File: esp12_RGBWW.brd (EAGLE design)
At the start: 49.5 x 50.5 mm, 22 parts

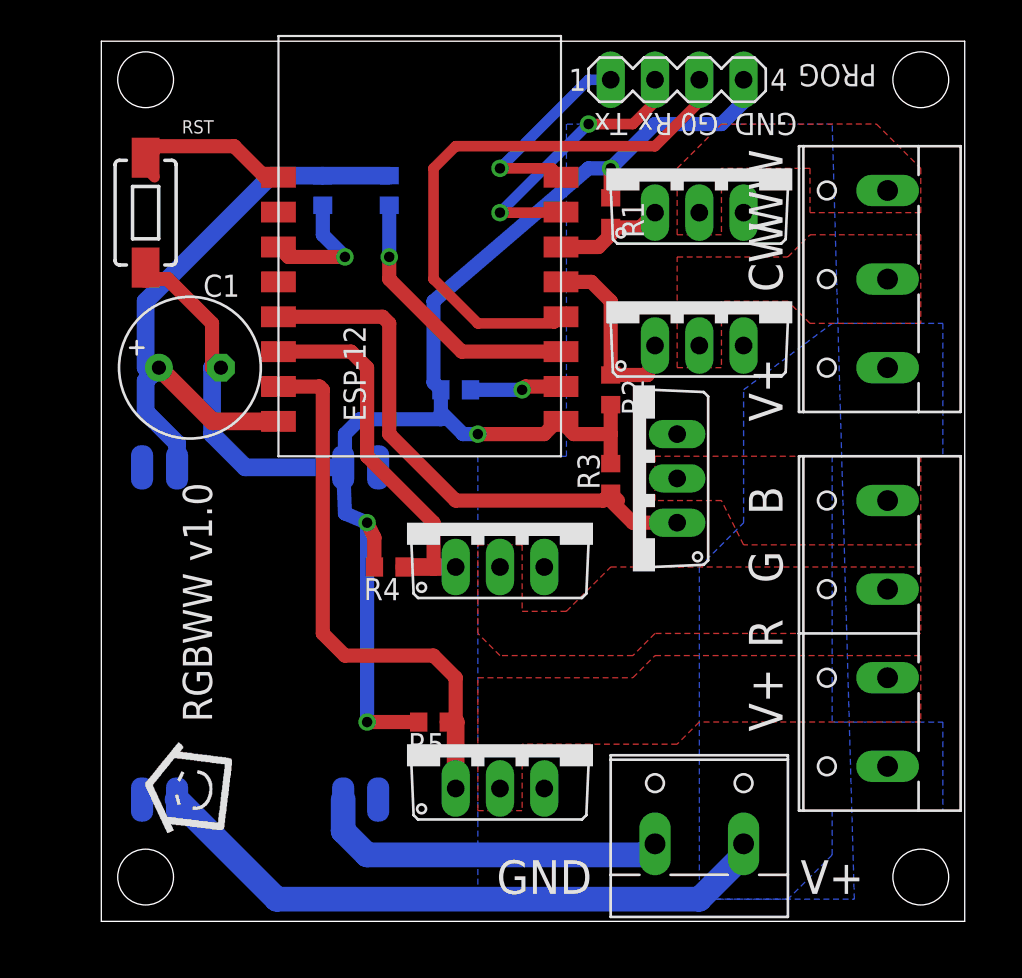
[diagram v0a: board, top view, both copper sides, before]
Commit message: added ADC and updated board layout
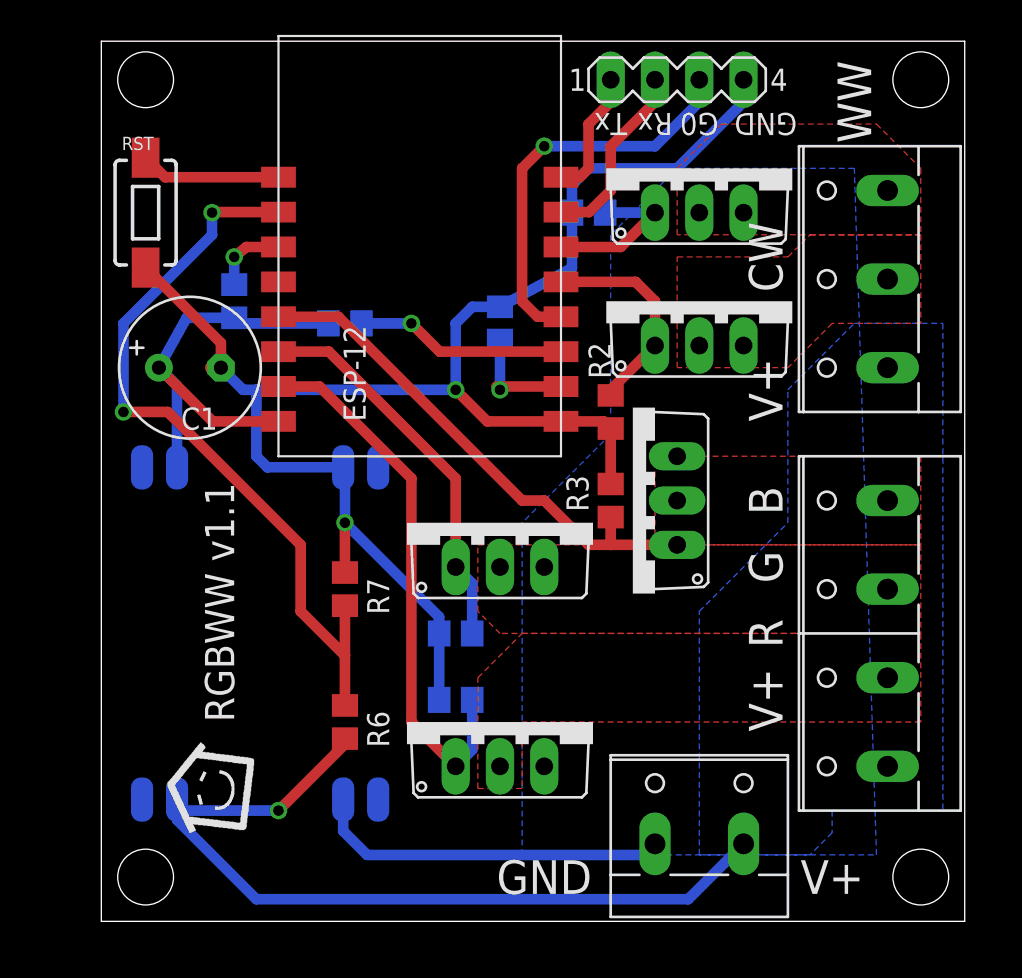
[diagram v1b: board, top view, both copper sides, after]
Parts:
- added R6: 10k, rcl:R0805
- added R7: 1k, rcl:R0805
- CH_PD, GPIO15, GPIO2, R1, R2, R3, R4, R5: device rcl:R0603 -> rcl:R0805
- moved CH_PD 8.13 mm to (7.62, 35.6), turned to 270 degrees
- moved GPIO2 8.03 mm to (14.0, 34.3), turned to 0 degrees
- moved R4 5.39 mm to (20.3, 16.5), flipped to the bottom, turned to 0 degrees
- moved GPIO15 4.58 mm to (22.9, 34.3), turned to 90 degrees
- moved R5 1.80 mm to (20.3, 12.7), flipped to the bottom, turned to 0 degrees
- moved U$1 1.27 mm to (8.89, 5.08)
- moved IRLZ44N-B 1.27 mm to (30.5, 24.1)
- moved IRLZ44N-R 1.27 mm to (22.9, 11.4)
- moved R1 1.27 mm to (27.9, 40.6), flipped to the bottom, turned to 180 degrees
- moved R2 1.27 mm to (29.2, 29.2)
- moved R3 1.27 mm to (29.2, 24.1)
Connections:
- new net N$21: ESP-12.10, R6.1, R7.2
- net +12V: now also R6.2
- net GND3.3V: now also R7.1
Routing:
- net N$21: track 0.00 -> 43.8 mm, vias 0 -> 2
- net +12V: track 36.5 -> 48.4 mm, vias 0 -> 1
- net N$20: track 36.2 -> 25.8 mm
- net N$9: track 33.0 -> 23.2 mm, vias 0 -> 1
- net N$5: track 16.3 -> 10.8 mm, vias 2 -> 0
- net N$8: track 12.2 -> 7.40 mm, vias 1 -> 0
- net GND3.3V: track 96.4 -> 91.8 mm, vias 4 -> 2
- net N$3: track 15.8 -> 12.1 mm
- net N$2: track 7.53 -> 4.33 mm
- net N$13: track 32.7 -> 29.9 mm
- net N$14: track 6.45 -> 9.07 mm
- net N$12: track 9.96 -> 8.08 mm
- net N$7: track 5.27 -> 6.82 mm
- net R4: track 21.4 -> 22.5 mm
- net N$1: track 11.4 -> 12.3 mm
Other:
- board text added: "RGBWW v1.1"
- board text removed: "RGBWW v1.0"

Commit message: v1.2
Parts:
- added C2: 100n, rcl:C0805
- added C3: (no value), resistor:E2,5-6
- added REST: 10k, rcl:R0805
- moved IRLZ44N-R 11.7 mm to (34.3, 14.0)
- moved IRLZ44N-G 11.5 mm to (34.3, 21.6)
- moved C1 10.2 mm to (5.08, 21.6), turned to 270 degrees
- moved VCC 10.2 mm to (24.1, 5.08)
- moved U$1 9.92 mm to (1.27, 11.4), turned to 0 degrees
- moved DC_CONVERTER 9.16 mm to (16.5, 21.6)
- moved R4 7.41 mm to (26.7, 20.3), flipped to the top, turned to 90 degrees
- moved R5 6.84 mm to (26.7, 15.2), flipped to the top
- moved R6 6.48 mm to (12.7, 17.8), turned to 180 degrees
- moved IRLZ44N-B 6.35 mm to (34.3, 29.2), turned to 0 degrees
- moved R2 4.58 mm to (26.7, 33.0)
- moved PROG 3.81 mm to (29.2, 48.3)
- moved ESP-12 3.81 mm to (6.35, 26.7)
- moved GPIO15 2.84 mm to (20.3, 35.6), turned to 180 degrees
- moved R7 2.84 mm to (12.7, 21.6), turned to 0 degrees
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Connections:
- removed net GND3.3V: C1.-, DC_CONVERTER.OUT-(2), ESP-12.1, GPIO15.2, PROG.4, R1.1, R2.2, R3.2, R4.2, R5.2, R7.1, RST.1
- removed net N$20: C1.+, CH_PD.2, DC_CONVERTER.OUT+(1), ESP-12.16, GPIO2.2
- new net +3V3: C1.+, C2.2, CH_PD.2, DC_CONVERTER.OUT+(1), ESP-12.16, GPIO2.2, REST.1
- net +12V: now also C3.+
- net GND: now also C1.-, C2.1, C3.-, DC_CONVERTER.OUT-(2), ESP-12.1, GPIO15.2, PROG.4, R1.1, R2.2, R3.2, R4.2, R5.2, R7.1, RST.1
- net N$12: now also REST.2
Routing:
- net GND: track 20.5 -> 175.1 mm, vias 0 -> 6
- net GND3.3V: track 91.8 -> 0.00 mm, vias 2 -> 0
- net +3V3: track 0.00 -> 37.5 mm
- net N$20: track 25.8 -> 0.00 mm
- net N$21: track 43.8 -> 30.2 mm
- net R4: track 22.5 -> 33.7 mm
- net +12V: track 48.4 -> 38.1 mm
- net N$23: track 31.6 -> 38.4 mm
- net N$12: track 8.08 -> 13.8 mm, vias 0 -> 1
- net N$3: track 12.1 -> 16.4 mm
- net N$7: track 6.82 -> 10.6 mm
- net N$2: track 4.33 -> 7.41 mm
- net N$25: track 9.07 -> 11.6 mm
- net N$24: track 12.3 -> 10.6 mm
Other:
- board text added: "RGBWW v1.2"
- board text removed: "RGBWW v1.1"

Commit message: small cosmetic corrections
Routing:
- net N$9: track 23.2 -> 23.9 mm
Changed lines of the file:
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@@
 <contactref element="PROG" pad="3"/>
 <wire x1="30.48" y1="46.99" x2="30.48" y2="48.26" width="0.6096" layer="16"/>
-<via x="22.86" y="45.72" extent="1-16" drill="0.6"/>
-<wire x1="22.86" y1="45.72" x2="29.21" y2="45.72" width="0.6096" layer="16"/>
+<via x="21.59" y="45.72" extent="1-16" drill="0.6"/>
+<wire x1="21.59" y1="45.72" x2="29.21" y2="45.72" width="0.6096" layer="16"/>
 <wire x1="29.21" y1="45.72" x2="30.48" y2="46.99" width="0.6096" layer="16"/>
 <wire x1="22.48" y1="34.67" x2="21.21" y2="34.67" width="0.6096" layer="1"/>
 <wire x1="21.21" y1="34.67" x2="20.32" y2="35.56" width="0.6096" layer="1"/>
-<wire x1="20.32" y1="35.56" x2="20.32" y2="43.18" width="0.6096" layer="1"/>
-<wire x1="20.32" y1="43.18" x2="22.86" y2="45.72" width="0.6096" layer="1"/>
+<wire x1="20.32" y1="35.56" x2="20.32" y2="44.45" width="0.6096" layer="1"/>
+<wire x1="20.32" y1="44.45" x2="21.59" y2="45.72" width="0.6096" layer="1"/>
 <wire x1="22.48" y1="34.67" x2="22.55" y2="34.67" width="0" layer="19" extent="1-1"/>
 </signal>
@@
 <contactref element="R5" pad="1"/>
 <wire x1="6.35" y1="30.67" x2="8.7" y2="30.67" width="0.6096" layer="1"/>
-<wire x1="8.7" y1="30.67" x2="16.51" y2="24.13" width="0.6096" layer="1"/>
-<wire x1="16.51" y1="24.13" x2="21.59" y2="24.13" width="0.6096" layer="1"/>
+<wire x1="8.7" y1="30.67" x2="15.24" y2="24.13" width="0.6096" layer="1"/>
+<wire x1="15.24" y1="24.13" x2="21.59" y2="24.13" width="0.6096" layer="1"/>
 <wire x1="21.59" y1="24.13" x2="22.86" y2="22.86" width="0.6096" layer="1"/>
 <wire x1="22.86" y1="22.86" x2="22.86" y2="19.05" width="0.6096" layer="1"/>
 <wire x1="31.75" y1="11.43" x2="26.67" y2="11.43" width="0.6096" layer="1"/>
 <wire x1="26.67" y1="11.43" x2="25.4" y2="12.7" width="0.6096" layer="1"/>
-<wire x1="25.4" y1="12.7" x2="25.4" y2="13.97" width="0.6096" layer="1"/>
-<wire x1="25.4" y1="13.97" x2="25.4" y2="14.92" width="0.6096" layer="1"/>
+<wire x1="25.4" y1="12.7" x2="25.4" y2="14.92" width="0.6096" layer="1"/>
 <wire x1="25.4" y1="14.92" x2="25.72" y2="15.24" width="0.6096" layer="1"/>
 <wire x1="25.4" y1="15.56" x2="25.72" y2="15.24" width="0.6096" layer="1"/>

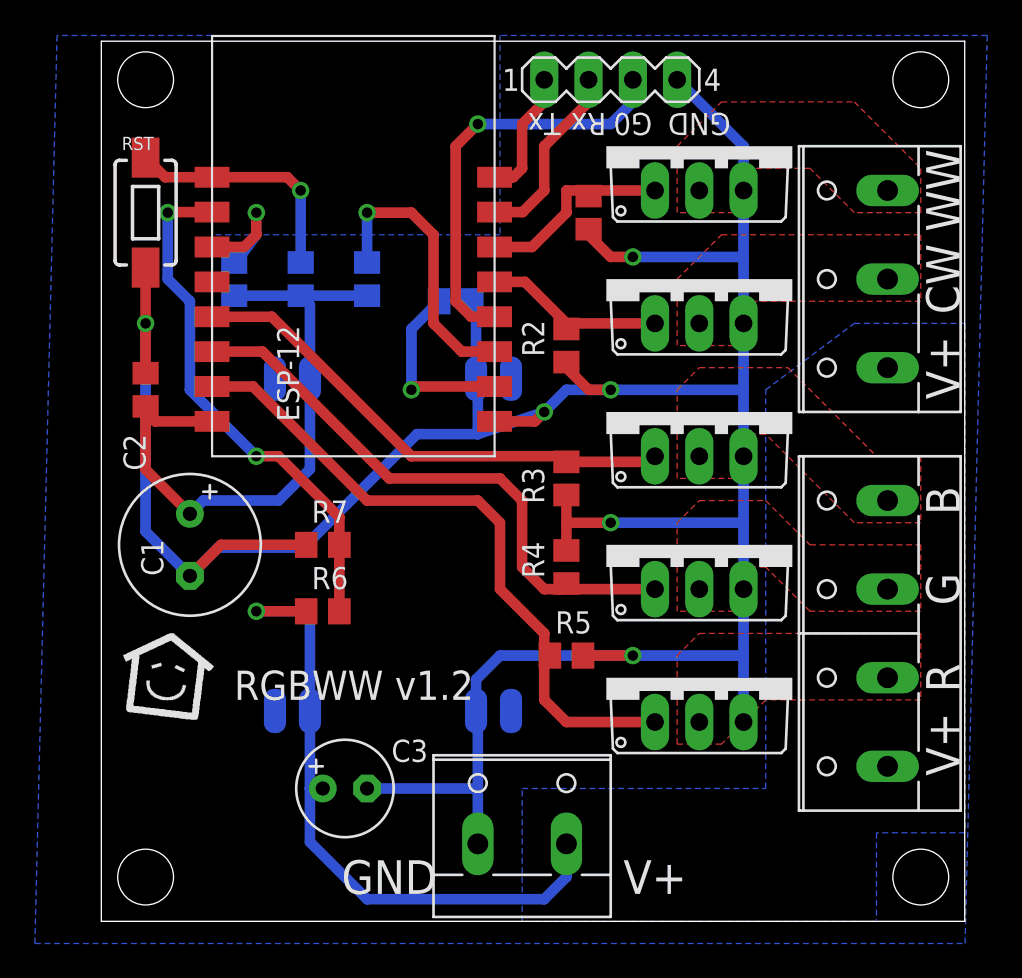
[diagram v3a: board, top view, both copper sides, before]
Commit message: MOSFET netclass renamed
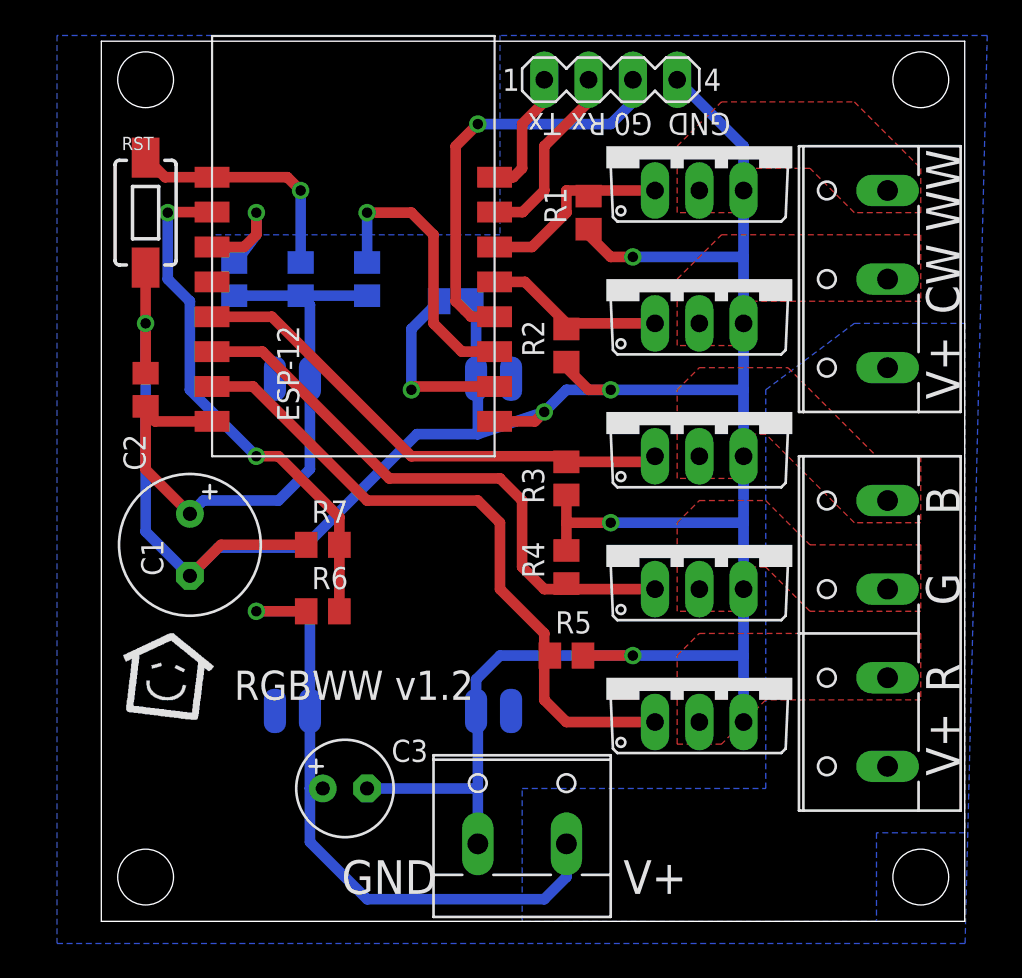
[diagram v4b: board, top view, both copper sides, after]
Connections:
- net N$10 renamed RGB-CW-OUT
- net N$11 renamed RGB-B-OUT
- net N$13 renamed RGB-B
- net N$15 renamed RGB-R-OUT
- net N$23 renamed RGB-R
- net N$24 renamed RGB-CW
- net N$25 renamed RGB-WW
- net N$4 renamed RGB-WW-OUT
- net N$6 renamed RGB-G-OUT
- net R4 renamed RGB-G
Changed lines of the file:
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@@
 </element>
 <element name="R1" library="rcl" package="R0805" value="10k" x="27.94" y="40.64" smashed="yes" rot="R90">
-<attribute name="VALUE" x="26.67" y="40.005" size="1.27" layer="27" rot="R90"/>
+<attribute name="NAME" x="26.67" y="40.005" size="1.27" layer="25" rot="R90"/>
 </element>
 <element name="R2" library="rcl" package="R0805" value="10k" x="26.67" y="33.02" smashed="yes" rot="R270">
@@
 <polygon width="0.254" layer="16" isolate="0.3048" thermals="no" rank="6">
 <vertex x="-2.54" y="50.8"/>
-<vertex x="-3.81" y="-1.27"/>
+<vertex x="-2.54" y="-1.27"/>
 <vertex x="49.53" y="-1.27"/>
 <vertex x="50.8" y="50.8"/>
@@
 <wire x1="15.24" y1="7.62" x2="21.59" y2="7.62" width="0.6096" layer="16"/>
 </signal>
-<signal name="N$11">
+<signal name="RGB-B-OUT">
 <contactref element="IRLZ44N-B" pad="C"/>
 <contactref element="RGB" pad="4"/>
@@
 <wire x1="17.78" y1="33.97" x2="19.37" y2="35.56" width="0.6096" layer="16"/>
 </signal>
-<signal name="N$13">
+<signal name="RGB-B">
 <contactref element="IRLZ44N-B" pad="B"/>
 <contactref element="R3" pad="1"/>
@@
 <wire x1="32.07" y1="26.35" x2="31.75" y2="26.67" width="0.6096" layer="1"/>
 </signal>
-<signal name="R4">
+<signal name="RGB-G">
 <contactref element="IRLZ44N-G" pad="B"/>
 <contactref element="R4" pad="1"/>
@@
 <wire x1="31.75" y1="19.05" x2="26.35" y2="19.05" width="0.6096" layer="1"/>
 </signal>
-<signal name="N$15">
+<signal name="RGB-R-OUT">
 <contactref element="IRLZ44N-R" pad="C"/>
 <contactref element="RGB" pad="2"/>
@@
 <wire x1="12.7" y1="7.62" x2="11.9634" y2="7.62" width="0.6096" layer="16"/>
 </signal>
-<signal name="N$10">
+<signal name="RGB-CW-OUT">
 <contactref element="IRLZ44N-CW" pad="C"/>
 <contactref element="W" pad="2"/>
@@
 </polygon>
 </signal>
-<signal name="N$6">
+<signal name="RGB-G-OUT">
 <contactref element="RGB" pad="3"/>
 <contactref element="IRLZ44N-G" pad="C"/>
@@
 <signal name="N$16">
 </signal>
-<signal name="N$4">
+<signal name="RGB-WW-OUT">
 <contactref element="W" pad="3"/>
 <contactref element="IRLZ44N-WW" pad="C"/>
@@
 <wire x1="2.54" y1="29.21" x2="2.54" y2="29.53" width="0" layer="19" extent="1-1"/>
 </signal>
-<signal name="N$23">
+<signal name="RGB-R">
 <contactref element="ESP-12" pad="15"/>
 <contactref element="IRLZ44N-R" pad="B"/>
@@
 <wire x1="25.4" y1="16.51" x2="25.4" y2="14.92" width="0.6096" layer="1"/>
 </signal>
-<signal name="N$24">
+<signal name="RGB-CW">
 <contactref element="ESP-12" pad="5"/>
 <contactref element="IRLZ44N-CW" pad="B"/>
@@
 <wire x1="26.99" y1="34.29" x2="26.67" y2="33.97" width="0.6096" layer="1"/>
 </signal>
-<signal name="N$25" class="5">
+<signal name="RGB-WW" class="5">
 <contactref element="ESP-12" pad="6"/>
 <contactref element="IRLZ44N-WW" pad="B"/>
